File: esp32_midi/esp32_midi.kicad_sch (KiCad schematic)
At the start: 15 parts, among them J1 USB_C_Receptacle_USB2.0, J2 5V-12V, U1 ESP32-S3-WROOM-2, U2 AMS1117-3.3

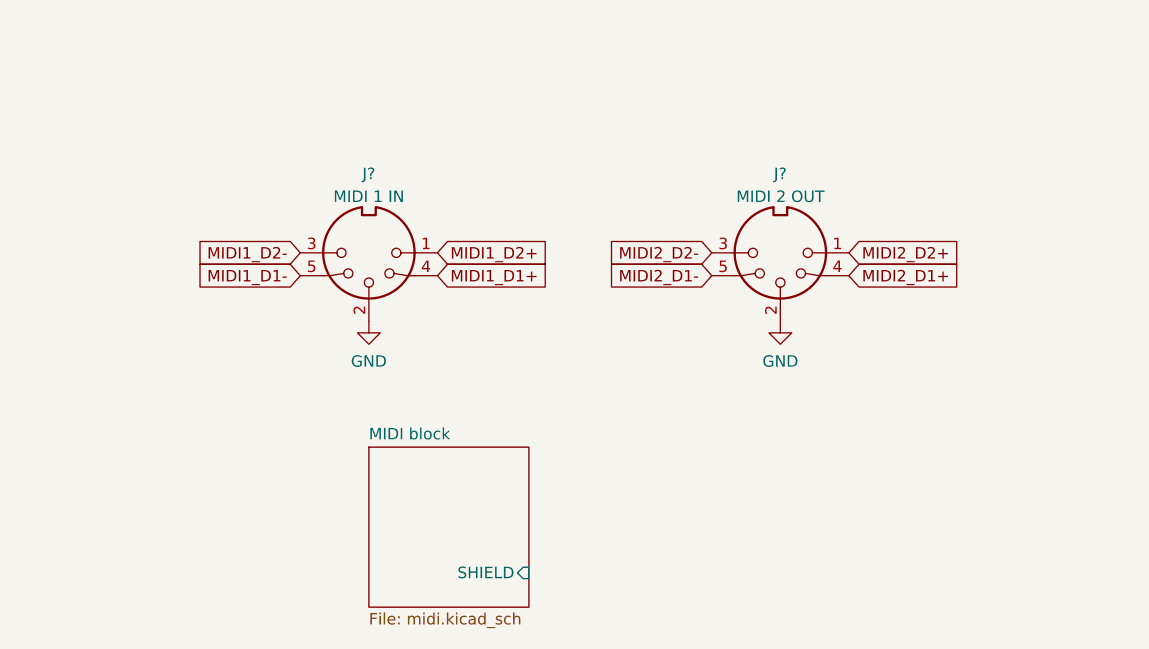
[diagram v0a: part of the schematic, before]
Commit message: added midi thru
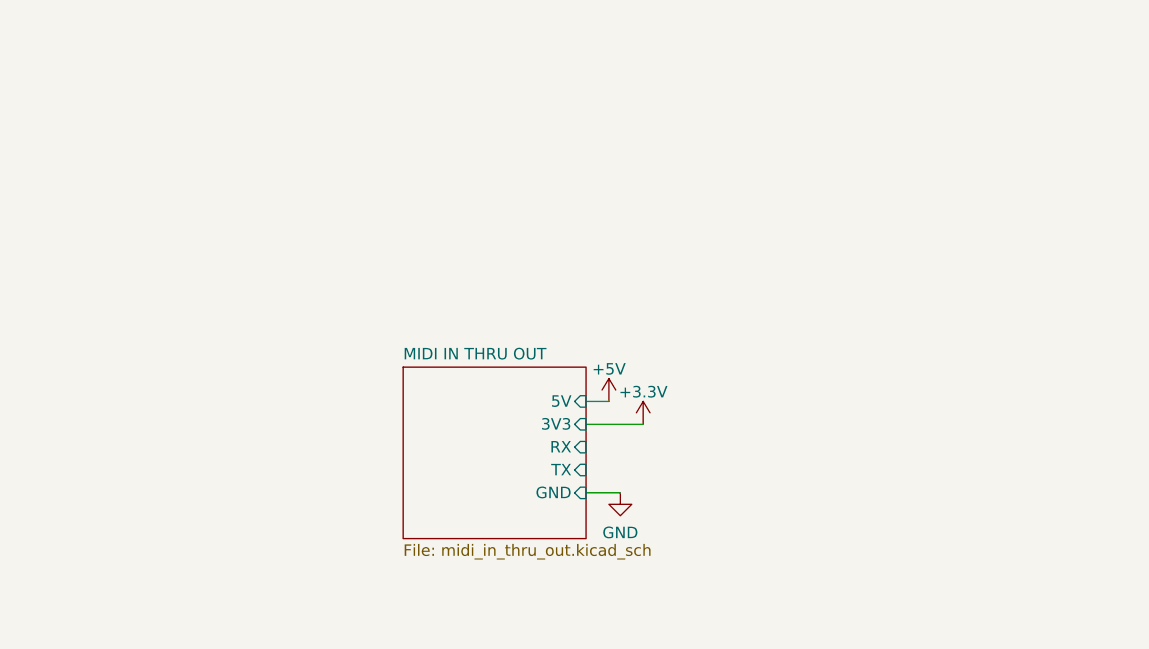
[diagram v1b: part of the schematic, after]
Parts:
- removed J?: MIDI 1 IN, symbol Connector:DIN-5_180degree
- removed J?: MIDI 2 OUT, symbol Connector:DIN-5_180degree
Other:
- removed sheet MIDI block
- added sheet MIDI IN THRU OUT (midi_in_thru_out.kicad_sch)

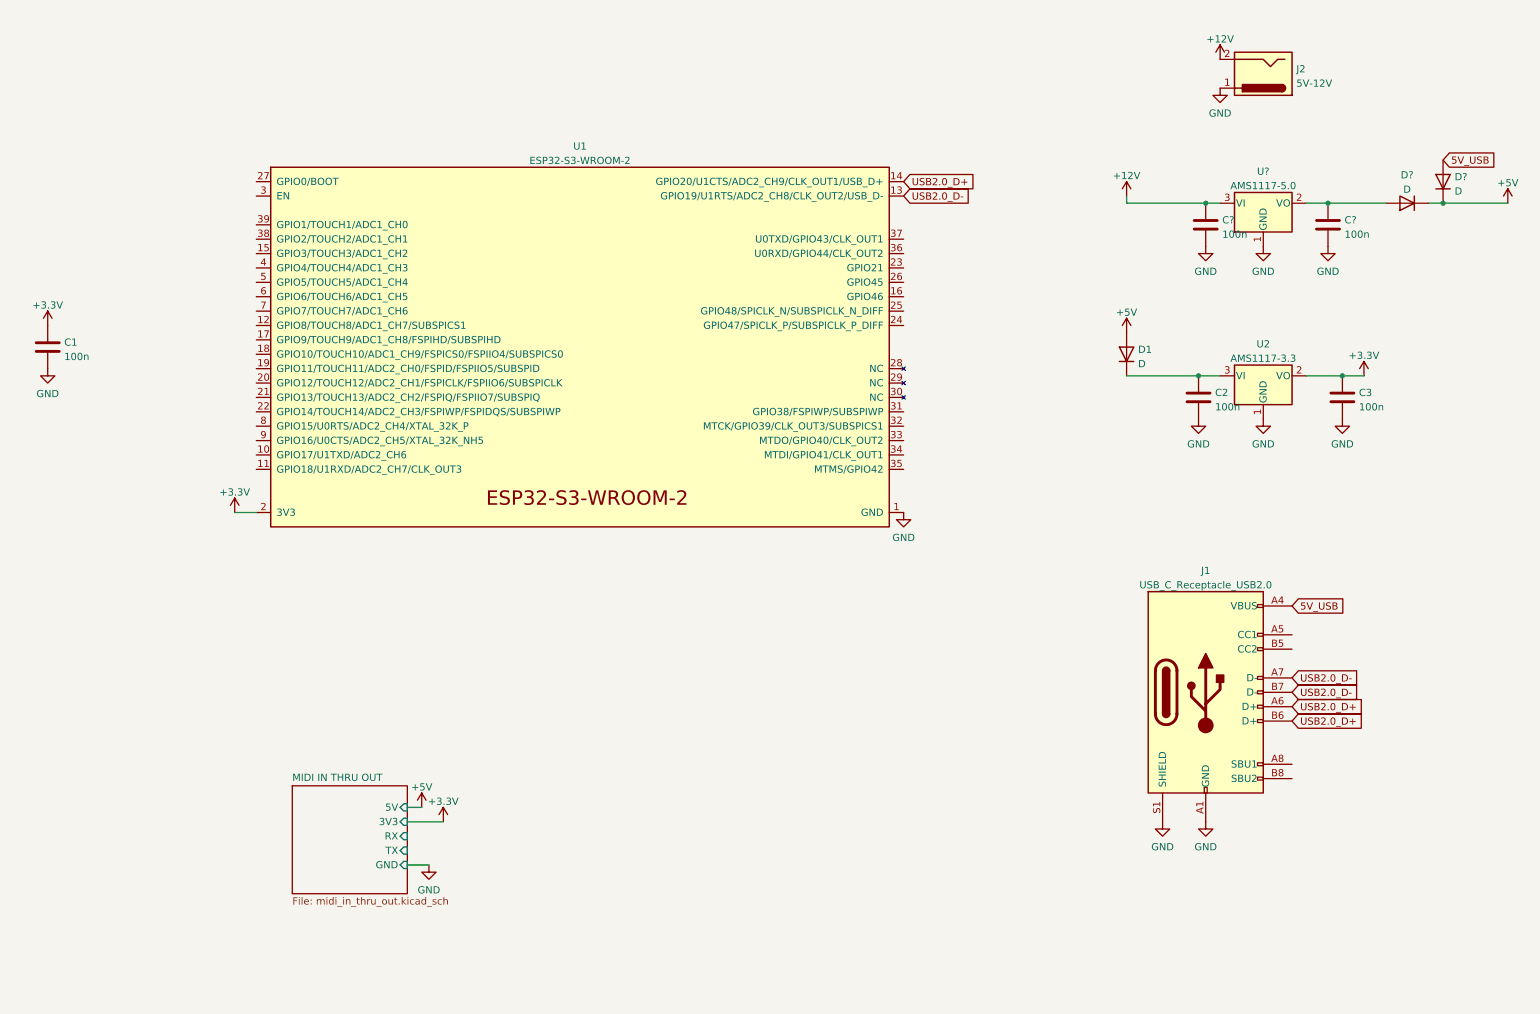
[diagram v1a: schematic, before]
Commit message: work in progress, added usb-c flasher, add display connector, add midi connections
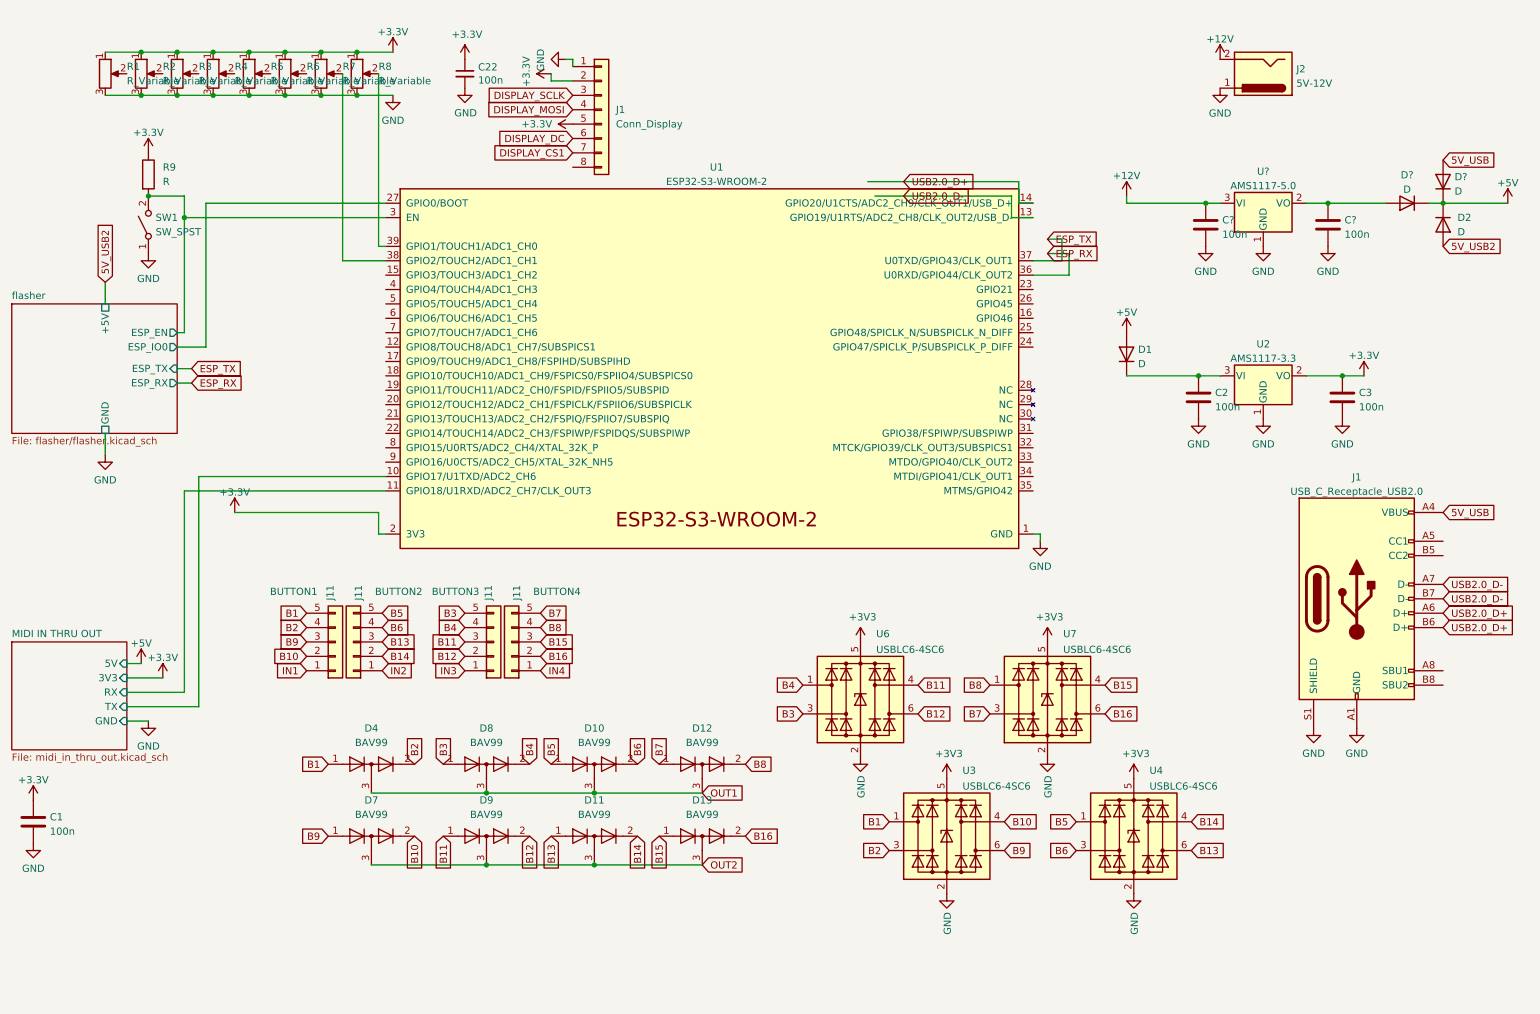
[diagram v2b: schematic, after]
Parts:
- added C22: 100n, Capacitor_SMD:C_0402_1005Metric, symbol Device:C_Small
- added D10, D11, D12, D13, D4, D7, D8, D9: BAV99, Package_TO_SOT_SMD:SOT-23, symbol Diode:BAV99
- added D2: D, symbol Device:D
- added J1: Conn_Display, Connector_PinHeader_2.54mm:PinHeader_1x08_P2.54mm_Vertical, symbol Connector_Generic:Conn_01x08
- added J11: BUTTON4, Connector_JST:JST_XH_B5B-XH-A_1x05_P2.50mm_Vertical, symbol Connector_Generic:Conn_01x05
- added J11: BUTTON1, Connector_JST:JST_XH_B5B-XH-A_1x05_P2.50mm_Vertical, symbol Connector_Generic:Conn_01x05
- added J11: BUTTON2, Connector_JST:JST_XH_B5B-XH-A_1x05_P2.50mm_Vertical, symbol Connector_Generic:Conn_01x05
- added J11: BUTTON3, Connector_JST:JST_XH_B5B-XH-A_1x05_P2.50mm_Vertical, symbol Connector_Generic:Conn_01x05
- added R1, R2, R3, R4, R5, R6, R7, R8: R_Variable, symbol Device:R_Potentiometer
- added R9: R, symbol Device:R
- added SW1: SW_SPST, symbol Switch:SW_SPST
- added U3, U4, U6, U7: USBLC6-4SC6, Package_TO_SOT_SMD:SOT-23-6, symbol Power_Protection:USBLC6-4SC6
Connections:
- net +3.3V: now also C22.1, J1.2 (Pin_2), J1.5 (Pin_5), R1.1, R2.1, R3.1, R4.1, R5.1, R6.1, R7.1, R8.1, R9.1
- net +5V: now also D2.1 (K)
- net GND: now also C22.2, J1.1 (Pin_1), R1.3, R2.3, R3.3, R4.3, R5.3, R6.3, R7.3, R8.3, SW1.1 (A), U3.2 (GND), U4.2 (GND), U6.2 (GND), U7.2 (GND)
- net MIDI IN THRU OUT/RX: now also U1.11 (GPIO18/U1RXD/ADC2_CH7/CLK_OUT3)
- net MIDI IN THRU OUT/TX: now also U1.10 (GPIO17/U1TXD/ADC2_CH6)
- net flasher/ESP_IO0: now reaches U1.27 (GPIO0/BOOT)
- net flasher/ESP_EN: now reaches U1.3 (EN)
- net flasher/ESP_EN: now also R9.2, SW1.2 (B)
- net ESP_RX: now reaches U1.36 (U0RXD/GPIO44/CLK_OUT2)
- net ESP_TX: now reaches U1.37 (U0TXD/GPIO43/CLK_OUT1)
- net at U1.38 (GPIO2/TOUCH2/ADC1_CH1): now also R7.2
- net at U1.39 (GPIO1/TOUCH1/ADC1_CH0): now also R8.2
- new net +3V3: U3.5 (VBUS), U4.5 (VBUS), U6.5 (VBUS), U7.5 (VBUS)
- new net 5V_USB2: D2.2 (A)
- new net B1: D4.1 (K), J11.5 (Pin_5), U3.1 (I/O1)
- new net B10: D7.2 (A), J11.2 (Pin_2), U3.4 (I/O3)
- new net B11: D9.1 (K), J11.3 (Pin_3), U6.4 (I/O3)
- new net B12: D9.2 (A), J11.2 (Pin_2), U6.6 (I/O4)
- new net B13: D11.1 (K), J11.3 (Pin_3), U4.6 (I/O4)
- new net B14: D11.2 (A), J11.2 (Pin_2), U4.4 (I/O3)
- new net B15: D13.1 (K), J11.3 (Pin_3), U7.4 (I/O3)
- new net B16: D13.2 (A), J11.2 (Pin_2), U7.6 (I/O4)
- new net B2: D4.2 (A), J11.4 (Pin_4), U3.3 (I/O2)
- new net B3: D8.1 (K), J11.5 (Pin_5), U6.3 (I/O2)
- new net B4: D8.2 (A), J11.4 (Pin_4), U6.1 (I/O1)
- new net B5: D10.1 (K), J11.5 (Pin_5), U4.1 (I/O1)
- new net B6: D10.2 (A), J11.4 (Pin_4), U4.3 (I/O2)
- new net B7: D12.1 (K), J11.5 (Pin_5), U7.3 (I/O2)
- new net B8: D12.2 (A), J11.4 (Pin_4), U7.1 (I/O1)
- new net B9: D7.1 (K), J11.3 (Pin_3), U3.6 (I/O4)
- new net DISPLAY_CS1: J1.7 (Pin_7)
- new net DISPLAY_DC: J1.6 (Pin_6)
- new net DISPLAY_MOSI: J1.4 (Pin_4)
- new net DISPLAY_SCLK: J1.3 (Pin_3)
- new net IN1: J11.1 (Pin_1)
- new net IN2: J11.1 (Pin_1)
- new net IN3: J11.1 (Pin_1)
- new net IN4: J11.1 (Pin_1)
- new net OUT1: D10.3 (K), D12.3 (K), D4.3 (K), D8.3 (K)
- new net OUT2: D11.3 (K), D13.3 (K), D7.3 (K), D9.3 (K)
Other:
- added sheet flasher (flasher/flasher.kicad_sch)
- moved on the sheet: C1, J1, U1

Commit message: Added analogorgie
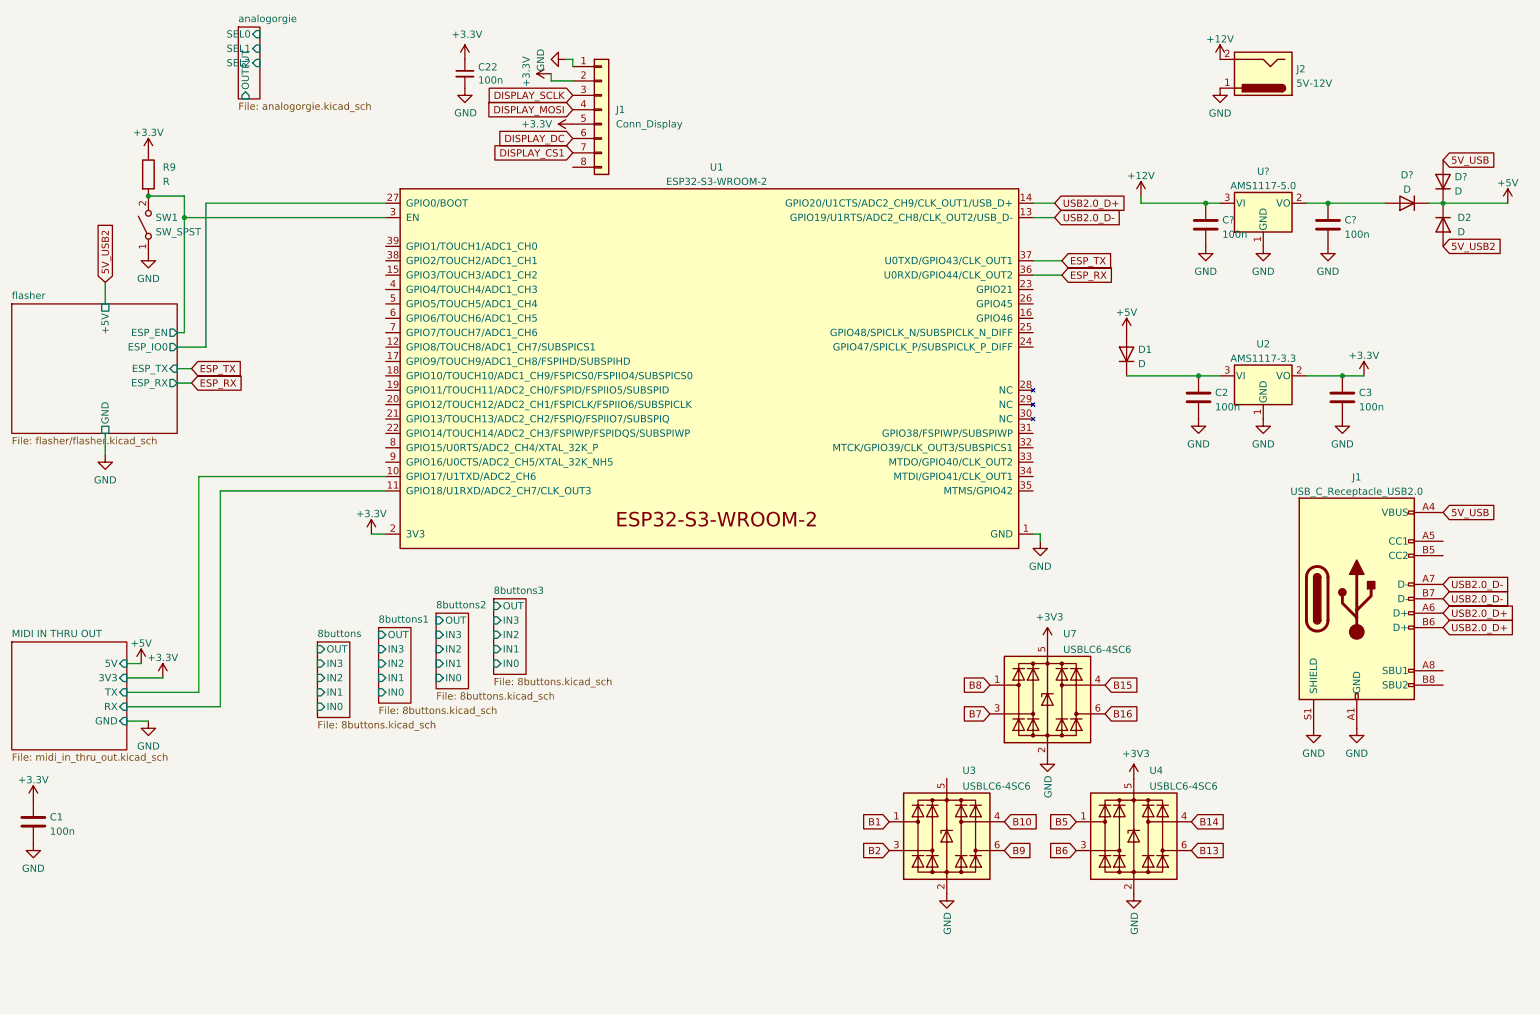
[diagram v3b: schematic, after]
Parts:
- removed D10, D11, D12, D13, D4, D7, D8, D9: BAV99, Package_TO_SOT_SMD:SOT-23, symbol Diode:BAV99
- removed J11: BUTTON4, Connector_JST:JST_XH_B5B-XH-A_1x05_P2.50mm_Vertical, symbol Connector_Generic:Conn_01x05
- removed J11: BUTTON1, Connector_JST:JST_XH_B5B-XH-A_1x05_P2.50mm_Vertical, symbol Connector_Generic:Conn_01x05
- removed J11: BUTTON2, Connector_JST:JST_XH_B5B-XH-A_1x05_P2.50mm_Vertical, symbol Connector_Generic:Conn_01x05
- removed J11: BUTTON3, Connector_JST:JST_XH_B5B-XH-A_1x05_P2.50mm_Vertical, symbol Connector_Generic:Conn_01x05
- removed R1, R2, R3, R4, R5, R6, R7, R8: R_Variable, symbol Device:R_Potentiometer
- removed U6: USBLC6-4SC6, Package_TO_SOT_SMD:SOT-23-6, symbol Power_Protection:USBLC6-4SC6
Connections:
- net +3V3: no longer U3.5 (VBUS)
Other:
- added sheet 8buttons (8buttons.kicad_sch)
- added sheet 8buttons1 (8buttons.kicad_sch)
- added sheet 8buttons2 (8buttons.kicad_sch)
- added sheet 8buttons3 (8buttons.kicad_sch)
- added sheet analogorgie (analogorgie.kicad_sch)

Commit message: More footprints applied
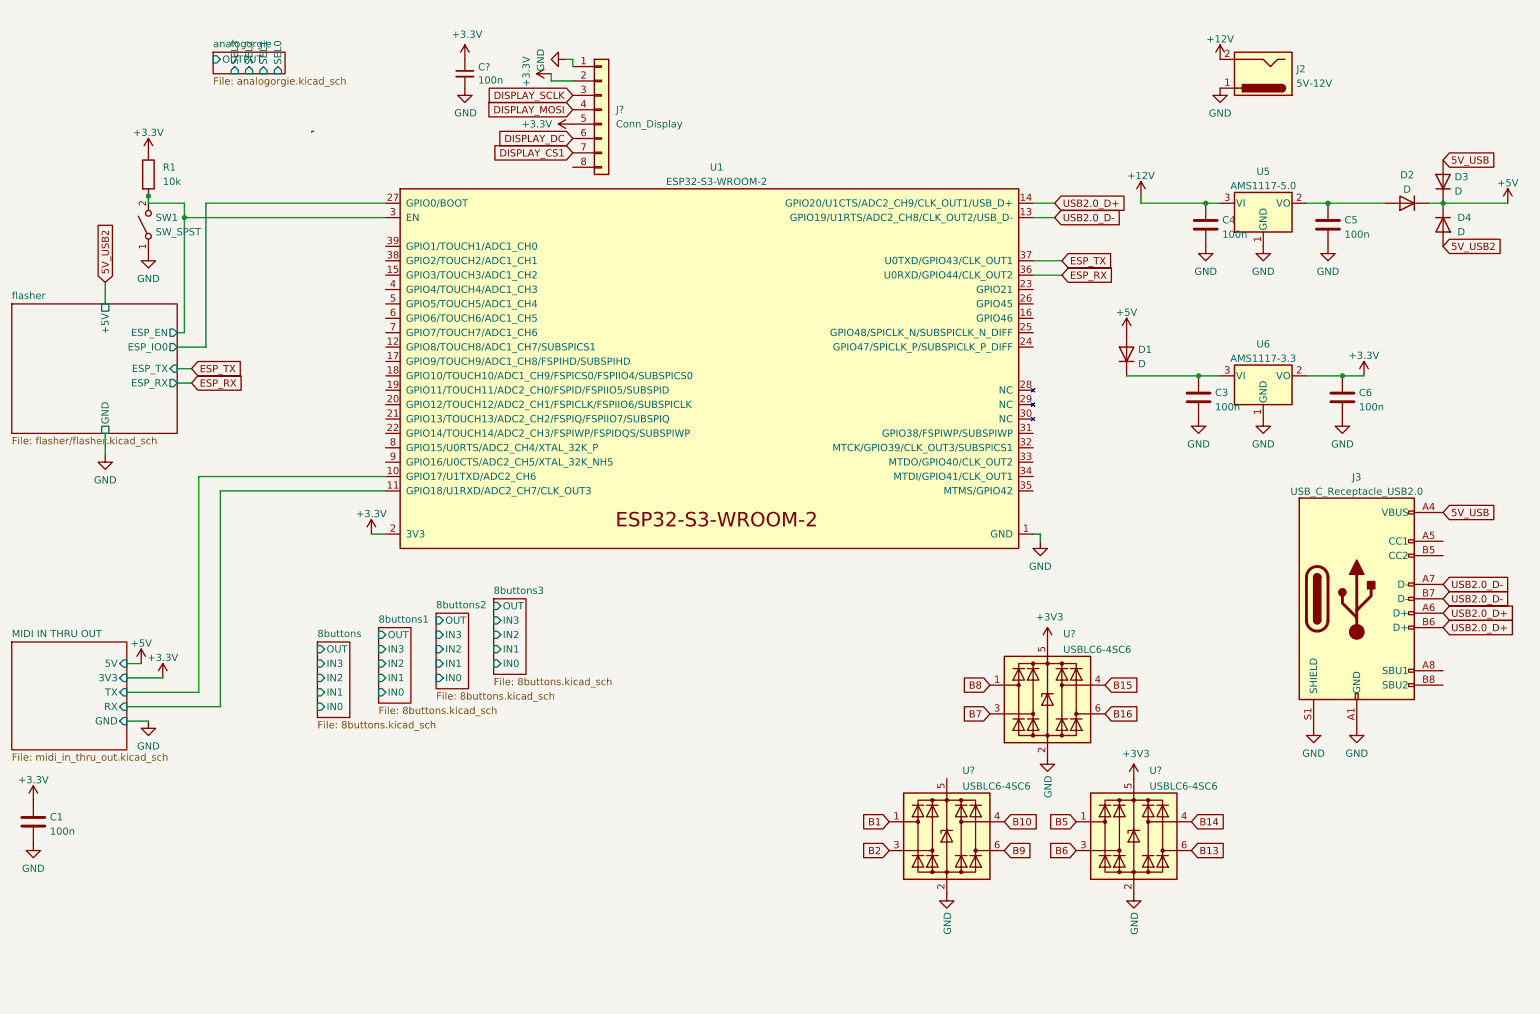
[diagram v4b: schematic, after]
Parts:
- C1: footprint (none) -> Capacitor_SMD:C_0402_1005Metric
- C3: renamed from C2; footprint (none) -> Capacitor_SMD:C_0402_1005Metric
- C4, C5: renamed from C?; footprint (none) -> Capacitor_SMD:C_0402_1005Metric
- C6: renamed from C3; footprint (none) -> Capacitor_SMD:C_0402_1005Metric
- D1: footprint (none) -> Diode_SMD:D_SOD-123
- D2, D3: renamed from D?; footprint (none) -> Diode_SMD:D_SOD-123
- D4: renamed from D2; footprint (none) -> Diode_SMD:D_SOD-123
- J2: footprint (none) -> Connector_BarrelJack:BarrelJack_Wuerth_6941xx301002
- J3: renamed from J1; footprint (none) -> Diode_SMD:D_SOD-123
- R1: renamed from R9; value R -> 10k; footprint (none) -> Resistor_SMD:R_0402_1005Metric
- gave numbers to parts that had none: 1
- renumbered C22 to C?, J1 to J?, U2 to U6, U4 to U?, U3 to U?, U7 to U?
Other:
- sheet analogorgie ports: added SEL3; removed none
